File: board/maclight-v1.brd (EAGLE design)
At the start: 105 x 16 mm, 52 parts, among them IC1 ATMEGA48/88/168-MU, Y1 20MHz

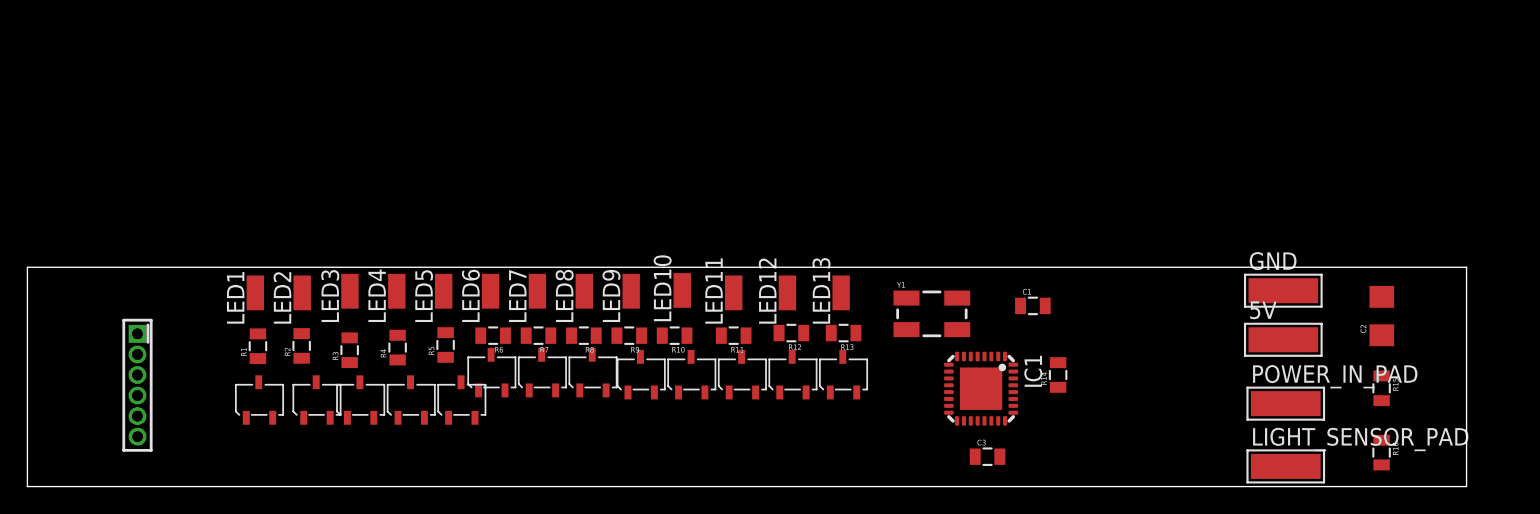
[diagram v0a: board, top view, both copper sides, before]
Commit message: Adding new board layout with LED driver (copied from Enterprise project)
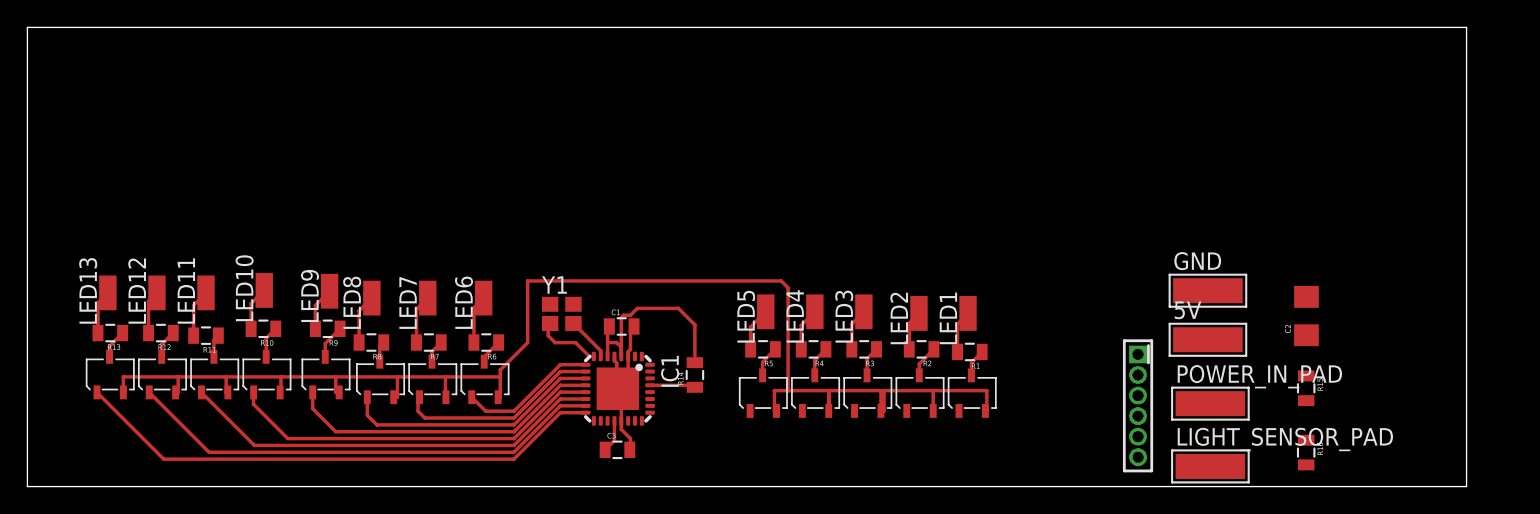
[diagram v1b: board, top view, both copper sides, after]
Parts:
- Y1: device SparkFun-FreqCtrl:CRYSTAL-SMD-5X3 -> crystal:FA-20H
- moved U$14 73.0 mm to (81.0, 9.64)
- moved LED13 53.5 mm to (5.87, 14.1)
- moved R13 53.5 mm to (6.05, 11.2)
- moved U$13 53.5 mm to (6.02, 8.18)
- moved LED1 52.0 mm to (68.6, 12.6)
- moved U$1 52.0 mm to (68.9, 6.83)
- moved R1 51.9 mm to (68.8, 9.82), turned to 180 degrees
- moved LED12 46.0 mm to (9.45, 14.1)
- moved R12 46.0 mm to (9.74, 11.2)
- moved U$12 46.0 mm to (9.83, 8.18)
- moved R2 45.2 mm to (65.2, 10.0), turned to 180 degrees
- moved LED2 45.0 mm to (65.0, 12.6)
- moved U$2 44.0 mm to (65.1, 6.83)
- moved LED11 38.5 mm to (13.0, 14.1)
- moved R11 38.5 mm to (13.0, 11.0)
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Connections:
- net GND: now also U$1.2, U$10.2, U$11.2, U$12.2, U$13.2, U$2.2, U$3.2, U$4.2, U$5.2, U$6.2, U$7.2, U$8.2, U$9.2
- net N$2: now also Y1.2; no longer Y1.3
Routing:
- net GND: track 0.00 -> 111.3 mm
- net MISO: track 0.00 -> 39.1 mm
- net MOSI: track 0.00 -> 35.1 mm
- net LED11: track 0.00 -> 31.0 mm
- net LED10: track 0.00 -> 27.5 mm
- net LED9: track 0.00 -> 23.2 mm
- net LED8: track 0.00 -> 18.9 mm
- net 5V: track 0.00 -> 15.8 mm
- net LED7: track 0.00 -> 14.9 mm
- net LED6: track 0.00 -> 10.1 mm
- net N$4: track 0.00 -> 4.91 mm
- net OUT8: track 0.00 -> 3.63 mm
- net OUT7: track 0.00 -> 3.58 mm
- net OUT6: track 0.00 -> 3.53 mm
- net OUT11: track 0.00 -> 3.49 mm
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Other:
- board size 105 x 16 mm -> 105 x 33.5 mm
